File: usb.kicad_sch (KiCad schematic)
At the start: 8 parts, among them U3 USB3343

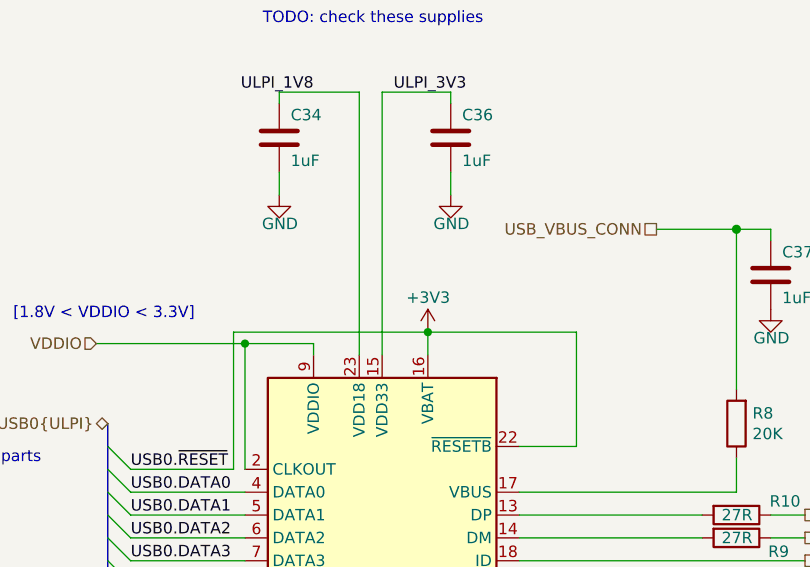
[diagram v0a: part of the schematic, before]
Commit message: kicad: fix LED PD, APMem, 1V8, USB ~RST short
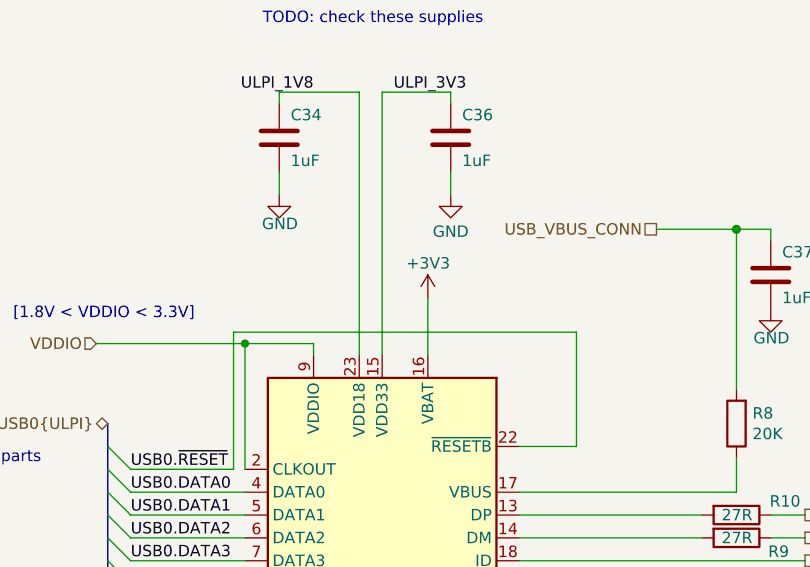
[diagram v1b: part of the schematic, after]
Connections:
- net +3V3: no longer U3.22 (~{RESETB})
- new net USB0.~{RESET}: U3.22 (~{RESETB})
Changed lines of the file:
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@@
-	)
-	(junction
-		(at 167.64 77.47)
-		(diameter 0)
-		(color 0 0 0 0)
 	)
 	(junction
@@
 		)
 	)
-	(wire
-		(pts
-			(xy 167.64 77.47) (xy 184.15 77.47)
-		)
-		(stroke
-			(width 0)
-			(type default)
-		)
-	)
 	(bus
 		(pts
@@
 	(wire
 		(pts
-			(xy 146.05 77.47) (xy 167.64 77.47)
+			(xy 146.05 77.47) (xy 184.15 77.47)
 		)
 		(stroke
@@
 	(wire
 		(pts
-			(xy 167.64 77.47) (xy 167.64 80.01)
+			(xy 167.64 73.66) (xy 167.64 80.01)
 		)
 		(stroke
@@
 		)
 		(property "Value" "GND"
-			(at 170.2562 65.4304 0)
+			(at 170.18 66.294 0)
 			(effects
 				(font
@@
 	(symbol
 		(lib_id "power:+3V3")
-		(at 167.64 77.47 0)
+		(at 167.64 73.66 0)
 		(unit 1)
 		(exclude_from_sim no)
@@
 		(dnp no)
 		(property "Reference" "#PWR022"
-			(at 167.64 81.28 0)
+			(at 167.64 77.47 0)
 			(effects
 				(font
@@
 		)
 		(property "Value" "+3V3"
-			(at 167.6781 73.6282 0)
+			(at 167.6781 69.8182 0)
 			(effects
 				(font
@@
 		)
 		(property "Footprint" ""
-			(at 167.64 77.47 0)
+			(at 167.64 73.66 0)
 			(effects
 				(font
@@
 		)
 		(property "Datasheet" ""
-			(at 167.64 77.47 0)
+			(at 167.64 73.66 0)
 			(effects
 				(font
@@
 		)
 		(property "Description" ""
-			(at 167.64 77.47 0)
-			(effects
-				(font
+			(at 167.64 73.66 0)
+			(effects
+				(font
